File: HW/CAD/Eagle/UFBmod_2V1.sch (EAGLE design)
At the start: 191 parts, among them T0551 MMBT2222, U0501 MIDAS_MCCOG21605B6W-FPTLWI, U0601 MAX5217, U0701 AT86RF215-ZU, U0711 ASVTX-13-D-26.000MHZ-I05-T, U0811 PE4259, U0821 RFX1010, U0881 B39871B3440U410, U0911 FT232HL, U1101 TPS53353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

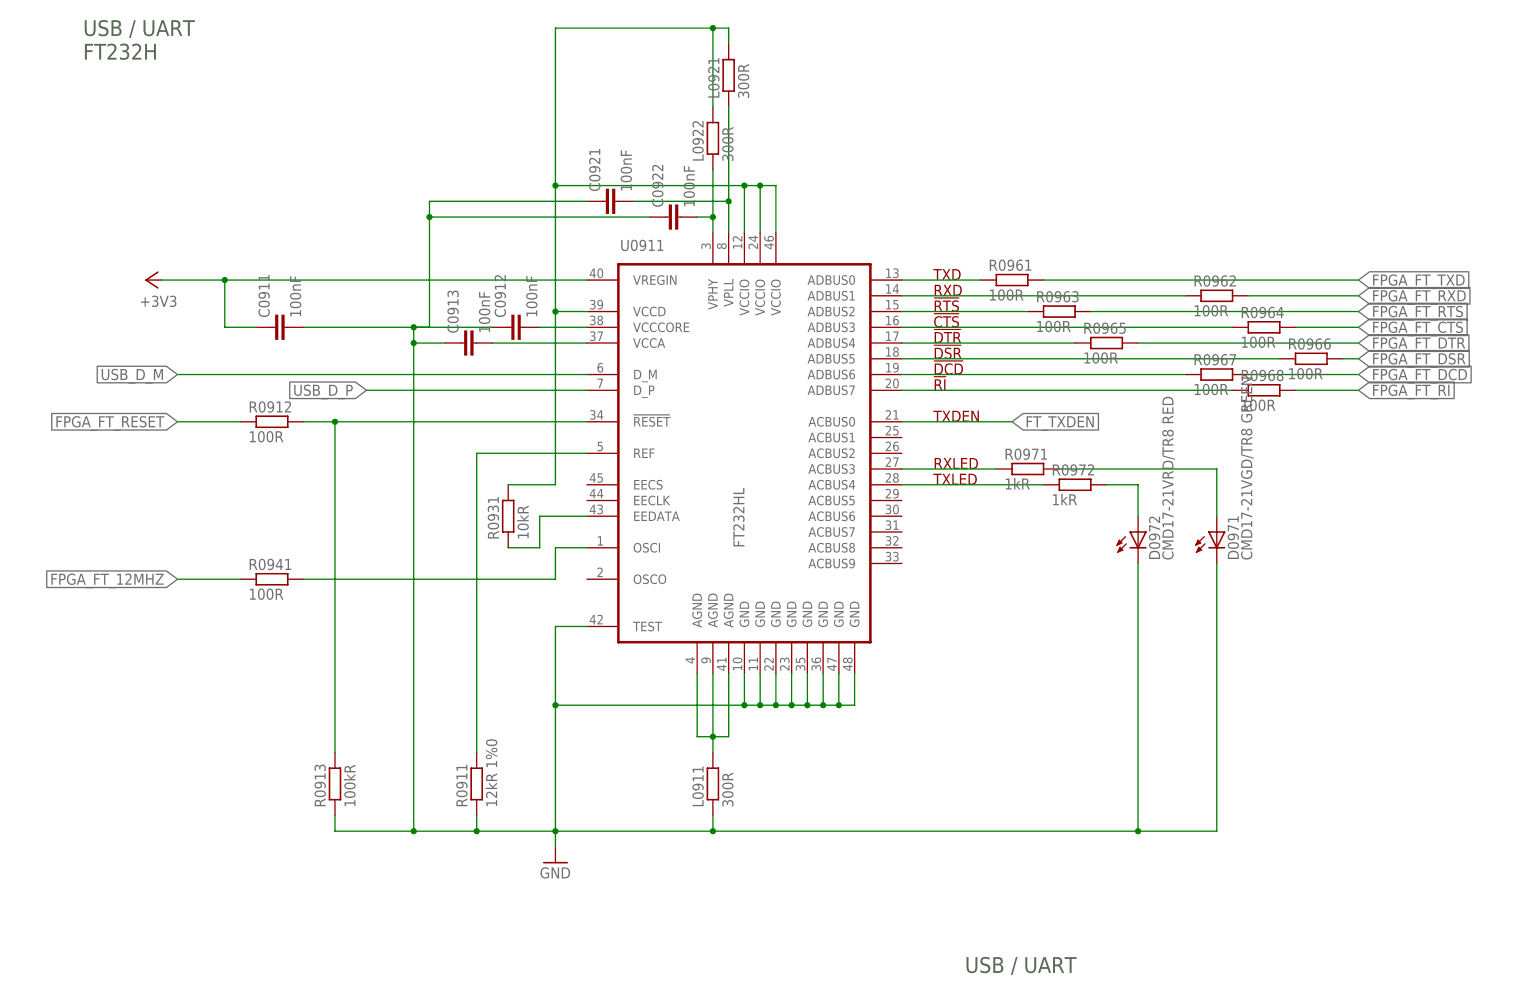
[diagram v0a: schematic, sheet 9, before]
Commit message: HW - Eagle - V2.1 update to current FPGA implementation
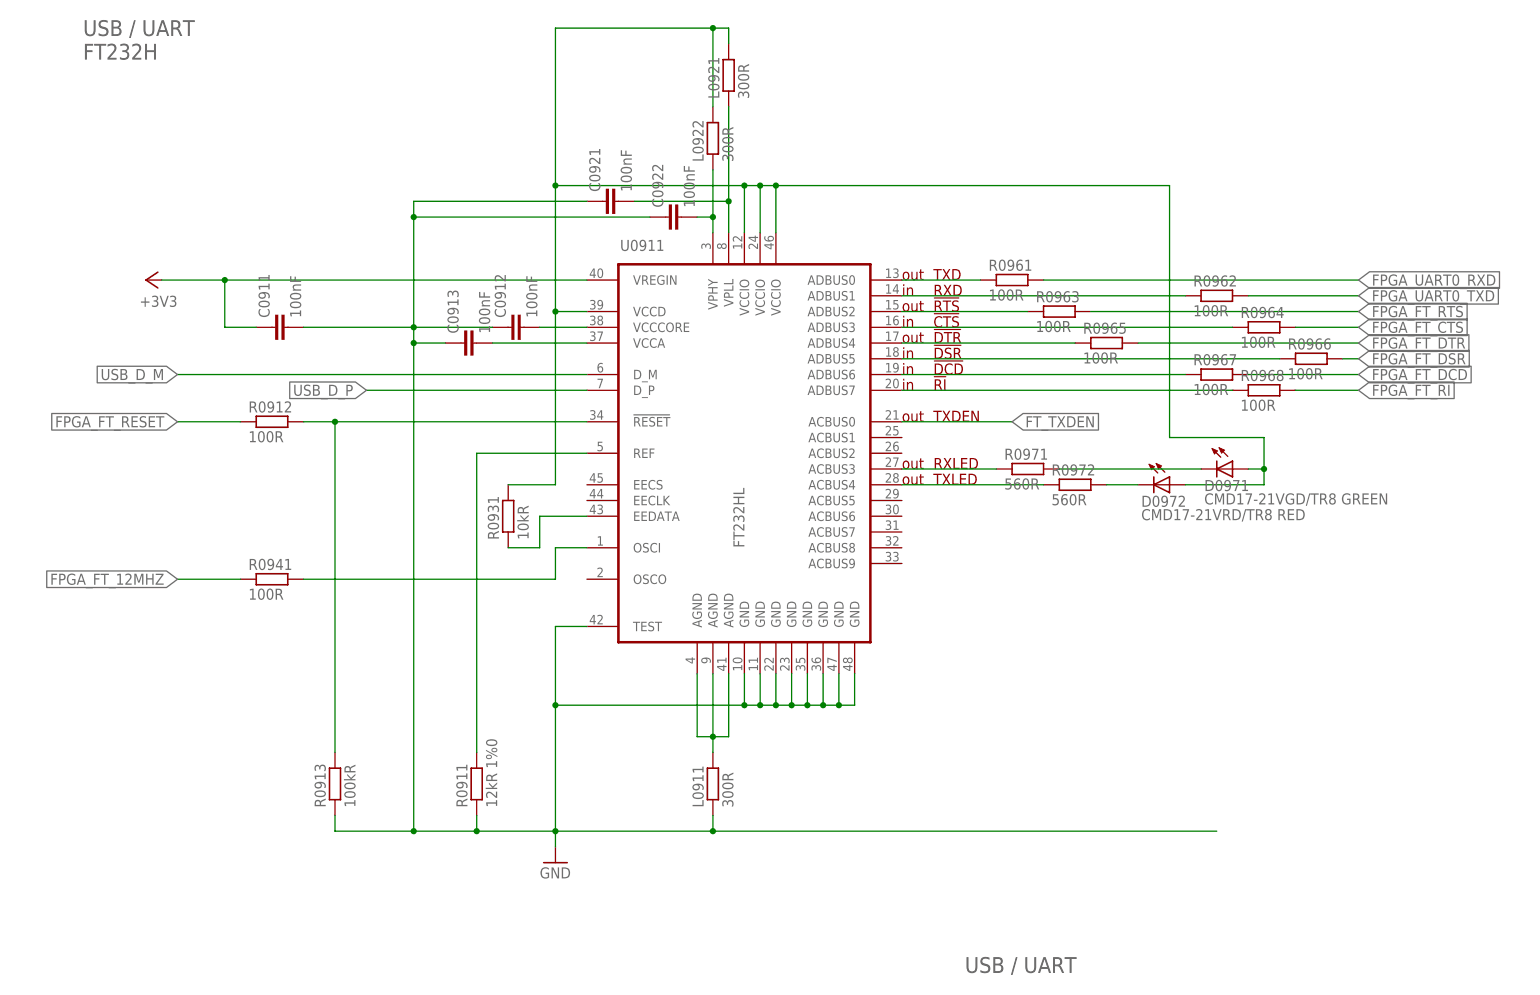
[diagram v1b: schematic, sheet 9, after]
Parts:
- R0971, R0972: value 1kR -> 560R
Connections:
- removed net FPGA_FT_RXD: JB2.B15_L6_P, R0962.2
- removed net FPGA_FT_TXD: JB2.B15_L6_N, R0961.2
- removed net UART0_RXD: JB1.B14_L24_MIO_P
- removed net UART0_TXD: JB1.B14_L18_MIO_N
- new net FPGA_UART0_RXD: JB1.B14_L24_MIO_P, R0961.2
- new net FPGA_UART0_TXD: JB1.B14_L18_MIO_N, R0962.2
- net FT_RXLED_D: now also D0971.C; no longer D0971.A
- net FT_TXLED_D: now also D0972.C; no longer D0972.A
- net FT_VCCD: now also D0971.A, D0972.A
- net GND: no longer D0971.C, D0972.C
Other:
- note added: "in"
- note added: "out"
- moved on the sheet: D0971, D0972
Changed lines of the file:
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@@
 <part name="R0967" library="df4iah_rcl" deviceset="R-EU_" device="R0402" value="100R"/>
 <part name="R0968" library="df4iah_rcl" deviceset="R-EU_" device="R0402" value="100R"/>
-<part name="R0971" library="df4iah_rcl" deviceset="R-EU_" device="R0402" value="1kR"/>
-<part name="R0972" library="df4iah_rcl" deviceset="R-EU_" device="R0402" value="1kR"/>
+<part name="R0971" library="df4iah_rcl" deviceset="R-EU_" device="R0402" value="560R"/>
+<part name="R0972" library="df4iah_rcl" deviceset="R-EU_" device="R0402" value="560R"/>
 <part name="D0972" library="df4iah_led" deviceset="LED" device="CHIP-LED0805" value="CMD17-21VRD/TR8  RED"/>
 <part name="D0971" library="df4iah_led" deviceset="LED" device="CHIP-LED0805" value="CMD17-21VGD/TR8  GREEN"/>
@@
 Left</text>
 <text x="22.86" y="162.56" size="2.54" layer="97" ratio="15">Trenz-Electronic TE0712-02-100-2C3  Left-Connector</text>
+<text x="91.44" y="45.72" size="1.778" layer="94">out</text>
+<text x="162.56" y="38.1" size="1.778" layer="94">in</text>
 </plain>
 <instances>
@@
 </segment>
 </net>
-<net name="UART0_TXD" class="0">
+<net name="FPGA_UART0_TXD" class="0">
 <segment>
 <pinref part="JB1" gate="G$1" pin="B14_L18_MIO_N"/>
@@
 </segment>
 </net>
-<net name="UART0_RXD" class="0">
+<net name="FPGA_UART0_RXD" class="0">
 <segment>
 <pinref part="JB1" gate="G$1" pin="B14_L24_MIO_P"/>
@@
 <wire x1="96.52" y1="40.64" x2="76.2" y2="40.64" width="0.1524" layer="91"/>
 <label x="76.2" y="40.64" size="1.778" layer="95" rot="R180" xref="yes"/>
-</segment>
-</net>
-<net name="FPGA_FT_TXD" class="0">
-<segment>
-<pinref part="JB2" gate="G$1" pin="B15_L6_N"/>
-<wire x1="162.56" y1="50.8" x2="182.88" y2="50.8" width="0.1524" layer="91"/>
-<label x="182.88" y="50.8" size="1.778" layer="95" xref="yes"/>
-</segment>
-</net>
-<net name="FPGA_FT_RXD" class="0">
-<segment>
-<pinref part="JB2" gate="G$1" pin="B15_L6_P"/>
-<wire x1="162.56" y1="48.26" x2="215.9" y2="48.26" width="0.1524" layer="91"/>
-<label x="215.9" y="48.26" size="1.778" layer="95" xref="yes"/>
 </segment>
 </net>
@@
 <text x="22.86" y="162.56" size="2.54" layer="97" ratio="15">USB / UART
 FT232H</text>
+<text x="154.94" y="124.46" size="1.778" layer="94">in</text>
+<text x="154.94" y="119.38" size="1.778" layer="94">in</text>
+<text x="154.94" y="114.3" size="1.778" layer="94">in</text>
+<text x="154.94" y="111.76" size="1.778" layer="94">in</text>
+<text x="154.94" y="109.22" size="1.778" layer="94">in</text>
+<text x="154.94" y="127" size="1.778" layer="94">out</text>
+<text x="154.94" y="121.92" size="1.778" layer="94">out</text>
+<text x="154.94" y="116.84" size="1.778" layer="94">out</text>
+<text x="154.94" y="104.14" size="1.778" layer="94">out</text>
+<text x="154.94" y="96.52" size="1.778" layer="94">out</text>
+<text x="154.94" y="93.98" size="1.778" layer="94">out</text>
 </plain>
 <instances>
@@
 <instance part="R0971" gate="G$1" x="175.26" y="96.52"/>
 <instance part="R0972" gate="G$1" x="182.88" y="93.98"/>
-<instance part="D0972" gate="G$1" x="193.04" y="86.36"/>
-<instance part="D0971" gate="G$1" x="205.74" y="86.36"/>
+<instance part="D0972" gate="G$1" x="198.12" y="93.98" rot="R270"/>
+<instance part="D0971" gate="G$1" x="208.28" y="96.52" rot="R270"/>
 </instances>
 <busses>
@@
 <wire x1="76.2" y1="119.38" x2="58.42" y2="119.38" width="0.1524" layer="91"/>
 <junction x="76.2" y="119.38"/>
-<wire x1="76.2" y1="119.38" x2="78.74" y2="119.38" width="0.1524" layer="91"/>
-<wire x1="78.74" y1="119.38" x2="78.74" y2="137.16" width="0.1524" layer="91"/>
+<wire x1="76.2" y1="119.38" x2="76.2" y2="137.16" width="0.1524" layer="91"/>
 <pinref part="C0921" gate="G$1" pin="1"/>
-<wire x1="78.74" y1="137.16" x2="78.74" y2="139.7" width="0.1524" layer="91"/>
-<wire x1="78.74" y1="139.7" x2="104.14" y2="139.7" width="0.1524" layer="91"/>
+<wire x1="76.2" y1="137.16" x2="76.2" y2="139.7" width="0.1524" layer="91"/>
+<wire x1="76.2" y1="139.7" x2="104.14" y2="139.7" width="0.1524" layer="91"/>
 <pinref part="C0922" gate="G$1" pin="1"/>
-<wire x1="78.74" y1="137.16" x2="114.3" y2="137.16" width="0.1524" layer="91"/>
-<junction x="78.74" y="137.16"/>
-<wire x1="124.46" y1="38.1" x2="193.04" y2="38.1" width="0.1524" layer="91"/>
+<wire x1="76.2" y1="137.16" x2="114.3" y2="137.16" width="0.1524" layer="91"/>
+<junction x="76.2" y="137.16"/>
+<wire x1="124.46" y1="38.1" x2="205.74" y2="38.1" width="0.1524" layer="91"/>
 <junction x="124.46" y="38.1"/>
-<pinref part="D0971" gate="G$1" pin="C"/>
-<wire x1="193.04" y1="38.1" x2="205.74" y2="38.1" width="0.1524" layer="91"/>
-<wire x1="205.74" y1="38.1" x2="205.74" y2="81.28" width="0.1524" layer="91"/>
-<pinref part="D0972" gate="G$1" pin="C"/>
-<wire x1="193.04" y1="38.1" x2="193.04" y2="81.28" width="0.1524" layer="91"/>
-<junction x="193.04" y="38.1"/>
 </segment>
 </net>
@@
 <wire x1="124.46" y1="167.64" x2="124.46" y2="154.94" width="0.1524" layer="91"/>
 <junction x="124.46" y="167.64"/>
+<wire x1="134.62" y1="142.24" x2="198.12" y2="142.24" width="0.1524" layer="91"/>
+<wire x1="198.12" y1="142.24" x2="198.12" y2="101.6" width="0.1524" layer="91"/>
+<junction x="134.62" y="142.24"/>
+<wire x1="198.12" y1="101.6" x2="213.36" y2="101.6" width="0.1524" layer="91"/>
+<wire x1="213.36" y1="101.6" x2="213.36" y2="96.52" width="0.1524" layer="91"/>
+<pinref part="D0971" gate="G$1" pin="A"/>
+<wire x1="213.36" y1="96.52" x2="210.82" y2="96.52" width="0.1524" layer="91"/>
+<wire x1="213.36" y1="96.52" x2="213.36" y2="93.98" width="0.1524" layer="91"/>
+<junction x="213.36" y="96.52"/>
+<pinref part="D0972" gate="G$1" pin="A"/>
+<wire x1="213.36" y1="93.98" x2="200.66" y2="93.98" width="0.1524" layer="91"/>
 </segment>
 </net>
@@
 </segment>
 </net>
-<net name="FPGA_FT_TXD" class="0">
+<net name="FPGA_UART0_RXD" class="0">
 <segment>
 <pinref part="R0961" gate="G$1" pin="2"/>
@@
 </segment>
 </net>
-<net name="FPGA_FT_RXD" class="0">
+<net name="FPGA_UART0_TXD" class="0">
 <segment>
 <pinref part="R0962" gate="G$1" pin="2"/>
@@
 <pinref part="R0972" gate="G$1" pin="2"/>
 <wire x1="187.96" y1="93.98" x2="193.04" y2="93.98" width="0.1524" layer="91"/>
-<wire x1="193.04" y1="93.98" x2="193.04" y2="88.9" width="0.1524" layer="91"/>
-<pinref part="D0972" gate="G$1" pin="A"/>
+<pinref part="D0972" gate="G$1" pin="C"/>
 </segment>
 </net>
@@
 <segment>
 <pinref part="R0971" gate="G$1" pin="2"/>
-<wire x1="180.34" y1="96.52" x2="205.74" y2="96.52" width="0.1524" layer="91"/>
-<wire x1="205.74" y1="96.52" x2="205.74" y2="88.9" width="0.1524" layer="91"/>
-<pinref part="D0971" gate="G$1" pin="A"/>
-</segment>
-</net>
+<wire x1="180.34" y1="96.52" x2="203.2" y2="96.52" width="0.1524" layer="91"/>
+<pinref part="D0971" gate="G$1" pin="C"/>
+</segment>
+</net>

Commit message: HW - Eagle - V2.1 some signals fixed
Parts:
- added C1321: 100nF, df4iah_rcl:C-EUC0402
- R1321: value 100R -> 1kR
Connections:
- net FPGA_RESET: now also C1321.2; no longer JB3.B13_L1_P
- net GND: now also C1321.1
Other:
- moved on the sheet: R1321, S1321
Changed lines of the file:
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@@
 <part name="TP1371" library="df4iah_connector" deviceset="TP" device="B1,27"/>
 <part name="S1321" library="df4iah_switch" deviceset="KSR223G_SMD_1POL" device=""/>
-<part name="R1321" library="df4iah_rcl" deviceset="R-EU_" device="R0402" value="100R"/>
+<part name="R1321" library="df4iah_rcl" deviceset="R-EU_" device="R0402" value="1kR"/>
 <part name="R0711" library="df4iah_rcl" deviceset="R-EU_" device="R0402" value="100R"/>
+<part name="C1321" library="df4iah_rcl" deviceset="C-EU" device="C0402" value="100nF"/>
+<part name="GND0001" library="df4iah_supply" deviceset="GND" device=""/>
 </parts>
 <sheets>
@@
 <net name="FPGA_RESET" class="0">
 <segment>
-<pinref part="JB3" gate="G$1" pin="B13_L1_P"/>
-<wire x1="144.78" y1="124.46" x2="144.78" y2="137.16" width="0.1524" layer="91"/>
-<wire x1="144.78" y1="137.16" x2="147.32" y2="137.16" width="0.1524" layer="91"/>
 <pinref part="JB3" gate="G$1" pin="B13_L1_N"/>
 <wire x1="147.32" y1="137.16" x2="147.32" y2="124.46" width="0.1524" layer="91"/>
-<wire x1="144.78" y1="137.16" x2="50.8" y2="137.16" width="0.1524" layer="91"/>
-<junction x="144.78" y="137.16"/>
+<wire x1="147.32" y1="137.16" x2="50.8" y2="137.16" width="0.1524" layer="91"/>
 <label x="50.8" y="137.16" size="1.778" layer="95" rot="R180" xref="yes"/>
 </segment>
@@
 <instance part="GND1381" gate="1" x="198.12" y="60.96"/>
 <instance part="TP1371" gate="G$1" x="220.98" y="81.28"/>
-<instance part="S1321" gate="G$1" x="114.3" y="53.34"/>
-<instance part="R1321" gate="G$1" x="114.3" y="40.64" rot="R90"/>
+<instance part="S1321" gate="G$1" x="114.3" y="55.88"/>
+<instance part="R1321" gate="G$1" x="114.3" y="43.18" rot="R90"/>
+<instance part="C1321" gate="G$1" x="114.3" y="27.94" smashed="yes" rot="R180">
+<attribute name="NAME" x="108.839" y="26.924" size="1.778" layer="95" rot="R90"/>
+<attribute name="VALUE" x="111.379" y="26.924" size="1.778" layer="96" rot="R90"/>
+</instance>
+<instance part="GND0001" gate="1" x="114.3" y="20.32"/>
 </instances>
 <busses>
@@
 <pinref part="GND1381" gate="1" pin="GND"/>
 </segment>
+<segment>
+<pinref part="GND0001" gate="1" pin="GND"/>
+<pinref part="C1321" gate="G$1" pin="1"/>
+<wire x1="114.3" y1="22.86" x2="114.3" y2="25.4" width="0.1524" layer="91"/>
+</segment>
 </net>
 <net name="USB_SHIELD" class="0">
@@
 <segment>
 <pinref part="S1321" gate="G$1" pin="S"/>
-<wire x1="114.3" y1="58.42" x2="114.3" y2="66.04" width="0.1524" layer="91"/>
-<label x="114.3" y="66.04" size="1.778" layer="95" rot="R90" xref="yes"/>
+<wire x1="114.3" y1="60.96" x2="114.3" y2="68.58" width="0.1524" layer="91"/>
+<label x="114.3" y="68.58" size="1.778" layer="95" rot="R90" xref="yes"/>
 </segment>
 </net>
@@
 <segment>
 <pinref part="R1321" gate="G$1" pin="1"/>
+<wire x1="114.3" y1="38.1" x2="114.3" y2="35.56" width="0.1524" layer="91"/>
+<wire x1="114.3" y1="35.56" x2="129.54" y2="35.56" width="0.1524" layer="91"/>
+<label x="129.54" y="35.56" size="1.778" layer="95" xref="yes"/>
+<pinref part="C1321" gate="G$1" pin="2"/>
 <wire x1="114.3" y1="35.56" x2="114.3" y2="33.02" width="0.1524" layer="91"/>
-<wire x1="114.3" y1="33.02" x2="129.54" y2="33.02" width="0.1524" layer="91"/>
-<label x="129.54" y="33.02" size="1.778" layer="95" xref="yes"/>
+<junction x="114.3" y="35.56"/>
 </segment>
 </net>
@@
 <pinref part="R1321" gate="G$1" pin="2"/>
 <pinref part="S1321" gate="G$1" pin="P"/>
-<wire x1="114.3" y1="45.72" x2="114.3" y2="48.26" width="0.1524" layer="91"/>
+<wire x1="114.3" y1="48.26" x2="114.3" y2="50.8" width="0.1524" layer="91"/>
 </segment>
 </net>

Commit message: HW - Eagle - V2.1 UART part fixed
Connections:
- net FPGA_FT_CTS renamed FPGA_FT_CTSN
- net FPGA_FT_DCD renamed FPGA_FT_DCDN
- net FPGA_FT_DSR renamed FPGA_FT_DSRN
- net FPGA_FT_DTR renamed FPGA_FT_DTRN
- net FPGA_FT_RESET renamed FPGA_FT_RESETN
- net FPGA_FT_RI renamed FPGA_FT_RIN
- net FPGA_FT_RTS renamed FPGA_FT_RTSN
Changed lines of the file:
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@@
 <text x="165.1" y="15.24" size="2.54" layer="97" ratio="15">Trenz-Electronic FPGA
 Right</text>
+<text x="162.56" y="27.94" size="1.778" layer="94">out</text>
+<text x="162.56" y="30.48" size="1.778" layer="94">out</text>
+<text x="162.56" y="33.02" size="1.778" layer="94">out</text>
+<text x="162.56" y="35.56" size="1.778" layer="94">out</text>
+<text x="162.56" y="43.18" size="1.778" layer="94">out</text>
+<text x="162.56" y="45.72" size="1.778" layer="94">in</text>
+<text x="162.56" y="38.1" size="1.778" layer="94">in</text>
+<text x="162.56" y="55.88" size="1.778" layer="94">out</text>
 </plain>
 <instances>
@@
 </segment>
 </net>
-<net name="FPGA_FT_DCD" class="0">
+<net name="FPGA_FT_DCDN" class="0">
 <segment>
 <pinref part="JB2" gate="G$1" pin="B15_L22_N"/>
@@
 </segment>
 </net>
-<net name="FPGA_FT_RI" class="0">
+<net name="FPGA_FT_RIN" class="0">
 <segment>
 <pinref part="JB2" gate="G$1" pin="B15_L22_P"/>
@@
 </segment>
 </net>
-<net name="FPGA_FT_RTS" class="0">
+<net name="FPGA_FT_RTSN" class="0">
 <segment>
 <pinref part="JB2" gate="G$1" pin="B15_L21_P"/>
@@
 </segment>
 </net>
-<net name="FPGA_FT_CTS" class="0">
+<net name="FPGA_FT_CTSN" class="0">
 <segment>
 <pinref part="JB2" gate="G$1" pin="B15_L21_N"/>
@@
 </segment>
 </net>
-<net name="FPGA_FT_DTR" class="0">
+<net name="FPGA_FT_DTRN" class="0">
 <segment>
 <pinref part="JB2" gate="G$1" pin="B15_L24_N"/>
@@
 </segment>
 </net>
-<net name="FPGA_FT_DSR" class="0">
+<net name="FPGA_FT_DSRN" class="0">
 <segment>
 <pinref part="JB2" gate="G$1" pin="B15_L24_P"/>
@@
 </segment>
 </net>
-<net name="FPGA_FT_RESET" class="0">
+<net name="FPGA_FT_RESETN" class="0">
 <segment>
 <pinref part="JB2" gate="G$1" pin="B15_L15_N"/>
@@
 </segment>
 </net>
-<net name="FPGA_FT_RESET" class="0">
+<net name="FPGA_FT_RESETN" class="0">
 <segment>
 <pinref part="R0912" gate="G$1" pin="1"/>
@@
 </segment>
 </net>
-<net name="FPGA_FT_RTS" class="0">
+<net name="FPGA_FT_RTSN" class="0">
 <segment>
 <pinref part="R0963" gate="G$1" pin="2"/>
@@
 </segment>
 </net>
-<net name="FPGA_FT_CTS" class="0">
+<net name="FPGA_FT_CTSN" class="0">
 <segment>
 <pinref part="R0964" gate="G$1" pin="2"/>
@@
 </segment>
 </net>
-<net name="FPGA_FT_DSR" class="0">
+<net name="FPGA_FT_DSRN" class="0">
 <segment>
 <pinref part="R0966" gate="G$1" pin="2"/>
@@
 </segment>
 </net>
-<net name="FPGA_FT_DTR" class="0">
+<net name="FPGA_FT_DTRN" class="0">
 <segment>
 <pinref part="R0965" gate="G$1" pin="2"/>
@@
 </segment>
 </net>
-<net name="FPGA_FT_DCD" class="0">
+<net name="FPGA_FT_DCDN" class="0">
 <segment>
 <pinref part="R0967" gate="G$1" pin="2"/>
@@
 </segment>
 </net>
-<net name="FPGA_FT_RI" class="0">
+<net name="FPGA_FT_RIN" class="0">
 <segment>
 <pinref part="R0968" gate="G$1" pin="2"/>

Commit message: HW - Eagle - V2.1 in/out/inout added
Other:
- note added: "inout"
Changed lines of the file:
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@@
 <text x="91.44" y="45.72" size="1.778" layer="94">out</text>
 <text x="162.56" y="38.1" size="1.778" layer="94">in</text>
+<text x="91.44" y="40.64" size="1.778" layer="94">in</text>
+<text x="91.44" y="50.8" size="1.778" layer="94">out</text>
+<text x="88.9" y="48.26" size="1.778" layer="94">inout</text>
+<text x="91.44" y="38.1" size="1.778" layer="94">out</text>
+<text x="91.44" y="35.56" size="1.778" layer="94">out</text>
+<text x="91.44" y="33.02" size="1.778" layer="94">out</text>
+<text x="91.44" y="30.48" size="1.778" layer="94">out</text>
+<text x="91.44" y="27.94" size="1.778" layer="94">out</text>
+<text x="162.56" y="149.86" size="1.778" layer="94">out</text>
+<text x="162.56" y="147.32" size="1.778" layer="94">out</text>
+<text x="162.56" y="142.24" size="1.778" layer="94">in</text>
+<text x="162.56" y="139.7" size="1.778" layer="94">in</text>
 </plain>
 <instances>
@@
 <text x="162.56" y="38.1" size="1.778" layer="94">in</text>
 <text x="162.56" y="55.88" size="1.778" layer="94">out</text>
+<text x="91.44" y="132.08" size="1.778" layer="94">out</text>
+<text x="91.44" y="137.16" size="1.778" layer="94">out</text>
+<text x="91.44" y="134.62" size="1.778" layer="94">out</text>
+<text x="91.44" y="127" size="1.778" layer="94">in</text>
+<text x="91.44" y="124.46" size="1.778" layer="94">in</text>
+<text x="91.44" y="121.92" size="1.778" layer="94">in</text>
+<text x="162.56" y="58.42" size="1.778" layer="94">out</text>
+<text x="91.44" y="30.48" size="1.778" layer="94">out</text>
+<text x="91.44" y="33.02" size="1.778" layer="94">in</text>
+<text x="91.44" y="40.64" size="1.778" layer="94">in</text>
+<text x="91.44" y="35.56" size="1.778" layer="94">in</text>
+<text x="91.44" y="27.94" size="1.778" layer="94">in</text>
+<text x="91.44" y="38.1" size="1.778" layer="94">out</text>
 </plain>
 <instances>
@@
 Top</text>
 <text x="22.86" y="27.94" size="2.54" layer="97" ratio="15">Module mount pads</text>
+<text x="147.32" y="124.46" size="1.778" layer="94" rot="R90">in</text>
 </plain>
 <instances>
